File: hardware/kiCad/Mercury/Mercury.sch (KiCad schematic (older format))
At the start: 13 parts

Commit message: VDDA
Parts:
- added C?: 1uF, symbol Device:C_Small
- added C?: 10nF, symbol Device:C_Small
- added L?: 39nH, symbol Device:L_Small
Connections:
- net +3.3VA: now also C?.1, C?.1, L?.2
- net +3V3: now also L?.1
- net GND: now also C?.2, C?.2
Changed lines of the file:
@@
 $EndComp
 Connection ~ 1900 1550
+$Comp
+L Device:L_Small L?
+U 1 1 5FE2984C
+P 5050 1150
+F 0 "L?" V 5250 1200 50  0000 C CNN
+F 1 "39nH" V 5150 1200 50  0000 C CNN
+F 2 "" H 5050 1150 50  0001 C CNN
+F 3 "~" H 5050 1150 50  0001 C CNN
+	1    5050 1150
+	0    -1   -1   0
+$EndComp
+$Comp
+L power:+3.3V #PWR?
+U 1 1 5FE29DC7
+P 4750 1100
+F 0 "#PWR?" H 4750 950 50  0001 C CNN
+F 1 "+3.3V" H 4765 1273 50  0000 C CNN
+F 2 "" H 4750 1100 50  0001 C CNN
+F 3 "" H 4750 1100 50  0001 C CNN
+	1    4750 1100
+	1    0    0    -1
+$EndComp
+Wire Wire Line
+	4750 1100 4750 1150
+Wire Wire Line
+	4750 1150 4950 1150
+$Comp
+L Device:C_Small C?
+U 1 1 5FE2B6A9
+P 5200 1250
+F 0 "C?" H 5150 1450 50  0000 L CNN
+F 1 "1uF" H 5100 1050 50  0000 L CNN
+F 2 "" H 5200 1250 50  0001 C CNN
+F 3 "~" H 5200 1250 50  0001 C CNN
+	1    5200 1250
+	1    0    0    -1
+$EndComp
+$Comp
+L Device:C_Small C?
+U 1 1 5FE2BF87
+P 5450 1250
+F 0 "C?" H 5400 1450 50  0000 L CNN
+F 1 "10nF" H 5350 1050 50  0000 L CNN
+F 2 "" H 5450 1250 50  0001 C CNN
+F 3 "~" H 5450 1250 50  0001 C CNN
+	1    5450 1250
+	1    0    0    -1
+$EndComp
+Wire Wire Line
+	5150 1150 5200 1150
+Wire Wire Line
+	5200 1150 5450 1150
+Connection ~ 5200 1150
+Wire Wire Line
+	5200 1350 5300 1350
+$Comp
+L power:+3.3VA #PWR?
+U 1 1 5FE3082E
+P 5600 1100
+F 0 "#PWR?" H 5600 950 50  0001 C CNN
+F 1 "+3.3VA" H 5615 1273 50  0000 C CNN
+F 2 "" H 5600 1100 50  0001 C CNN
+F 3 "" H 5600 1100 50  0001 C CNN
+	1    5600 1100
+	1    0    0    -1
+$EndComp
+Wire Wire Line
+	5450 1150 5600 1150
+Wire Wire Line
+	5600 1150 5600 1100
+Connection ~ 5450 1150
+$Comp
+L power:GND #PWR?
+U 1 1 5FE32675
+P 5300 1450
+F 0 "#PWR?" H 5300 1200 50  0001 C CNN
+F 1 "GND" H 5305 1277 50  0000 C CNN
+F 2 "" H 5300 1450 50  0001 C CNN
+F 3 "" H 5300 1450 50  0001 C CNN
+	1    5300 1450
+	1    0    0    -1
+$EndComp
+Wire Wire Line
+	5300 1450 5300 1350
+Connection ~ 5300 1350
+Wire Wire Line
+	5300 1350 5450 1350
 $EndSCHEMATC

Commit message: Clock
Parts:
- added C? (x2): 12pF, symbol Device:C_Small
- added R?: 47, symbol Device:R_Small
- added Y?: HSE 16MHz, symbol Device:Crystal_GND24_Small
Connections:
- net GND: now also C?.2, C?.2, Y?.2, Y?.4
- net HSE_OSC_IN: now also C?.1, Y?.1
- net HSE_OSC_OUT: now also R?.2
- new net: C?.1, R?.1, Y?.3
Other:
- moved on the sheet: C?, L?, R?, SW?, U?

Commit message: Added Connectors
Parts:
- added C? (x4): 22uF, symbol Device:C_Small
- added D?: GREEN_LED, symbol Device:LED
- added J?: Battery Input, symbol Connector:Screw_Terminal_01x02
- added J?: SWD, symbol Connector_Generic:Conn_02x05_Odd_Even
- added J? (x2): I2C1, symbol Connector_Generic:Conn_01x04
- added J?: I2C2, symbol Connector_Generic:Conn_01x04
- added J?: USB_C_Receptacle_USB2.0, symbol Connector:USB_C_Receptacle_USB2.0
- added Q?: AO3401A, Package_TO_SOT_SMD:SOT-23, symbol Transistor_FET:AO3401A
- added R?: 1k, symbol Device:R_Small
- added R? (x4): 4k7, symbol Device:R_Small
- added U?: AMS1117-3.3, Package_TO_SOT_SMD:SOT-223-3_TabPin2, symbol Regulator_Linear:AMS1117-3.3
- added U?: AMS1117-5.0, Package_TO_SOT_SMD:SOT-223-3_TabPin2, symbol Regulator_Linear:AMS1117-5.0
- added U?: TUSB320, Package_DFN_QFN:Texas_X2QFN-12_1.6x1.6mm_P0.4mm, symbol Interface_USB:TUSB320
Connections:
- net labels added: +5V, STATUS_LED, V+, Vin
- wire segments 73 -> 127
- no-connect marks 0 -> 2

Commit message: USB CONNECTOR MICROB
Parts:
- removed J?: USB_C_Receptacle_USB2.0, symbol Connector:USB_C_Receptacle_USB2.0
- removed U?: TUSB320, Package_DFN_QFN:Texas_X2QFN-12_1.6x1.6mm_P0.4mm, symbol Interface_USB:TUSB320
- added D?: RED_LED, symbol Device:LED
- added D?: ORANGE_LED, symbol Device:LED
- added J?: USB_B_Micro, symbol Connector:USB_B_Micro
- added R? (x2): 10, symbol Device:R_Small
- added R? (x10): 22, symbol Device:R_Small
- added R? (x2): 1k, symbol Device:R_Small
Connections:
- wire segments 127 -> 139
- no-connect marks 2 -> 6
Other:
- moved on the sheet: D?, J?, R?

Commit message: Peripherals Added
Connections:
- net ALT_INT_2: now reaches U?.45 (PE14)
- net ALT_INT_1: now reaches U?.46 (PE15)
- net FLASH_CS: now reaches U?.51 (PB12)
- net IMU_INT: now reaches U?.91 (PB5)
- no-connect marks 6 -> 5
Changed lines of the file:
@@
 $Descr USLetter 11000 8500
 encoding utf-8
-Sheet 1 1
+Sheet 1 2
 Title "Mercury Avionics Package"
 Date "2020-12-21"
@@
 	0    -1   -1   0
 $EndComp
-NoConn ~ 800  6125
 $Comp
 L Device:LED D?
@@
 	-1   0    0    1
 $EndComp
+$Sheet
+S 6050 4975 1600 800
+U 5FE81F4B
+F0 "peripherals" 50
+F1 "peripherals.sch" 50
+$EndSheet
+Text GLabel 4300 4000 2    50   Input ~ 0
+IMU_INT
+Text GLabel 4300 4700 2    50   Input ~ 0
+FLASH_CS
+Text GLabel 2500 4900 0    50   Input ~ 0
+ALT_INT_2
+Text GLabel 2500 5000 0    50   Input ~ 0
+ALT_INT_1
 $EndSCHEMATC

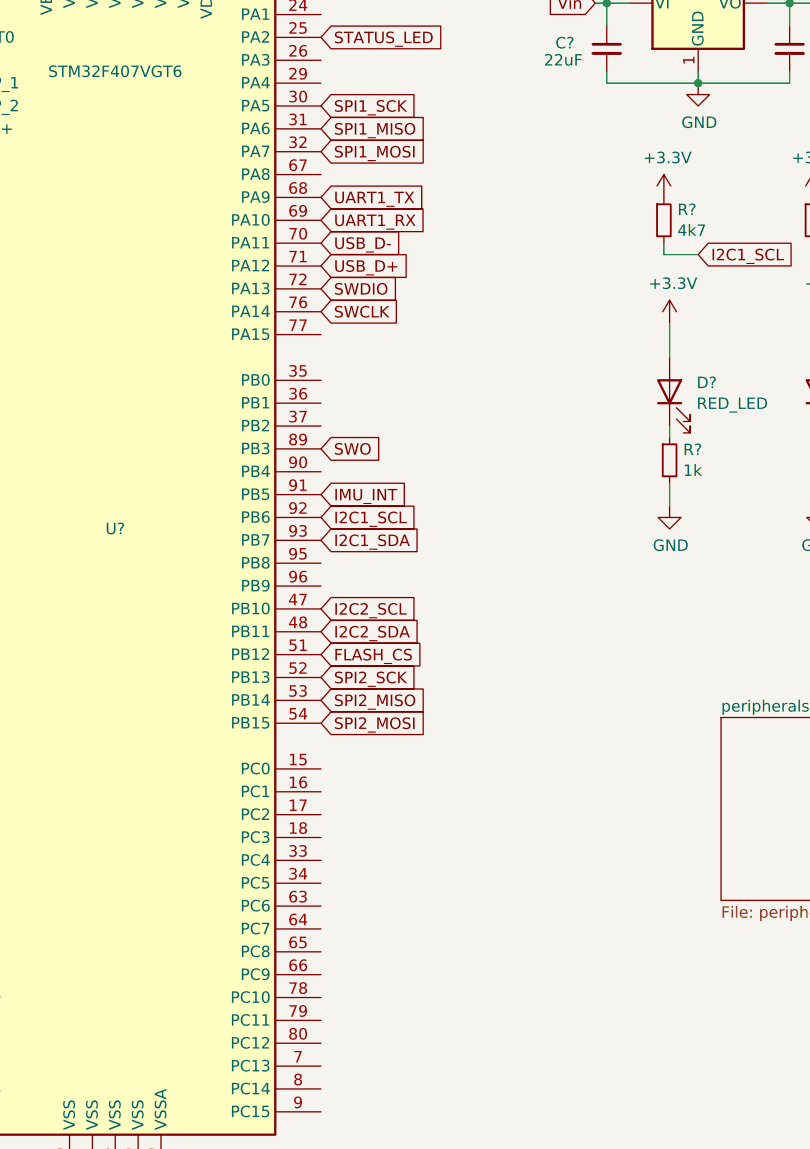
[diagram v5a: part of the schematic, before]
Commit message: GPS MODULE ADDED
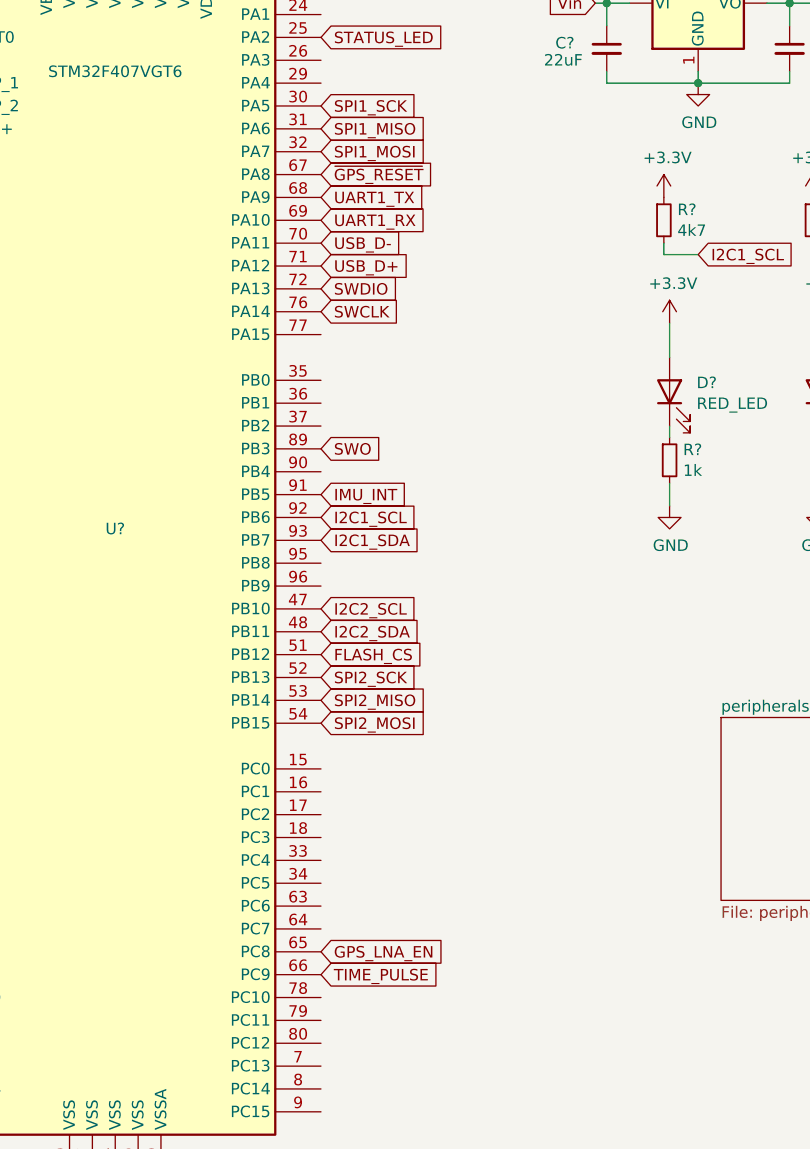
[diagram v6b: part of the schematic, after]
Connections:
- net GPS_LNA_EN: now reaches U?.65 (PC8)
- net TIME_PULSE: now reaches U?.66 (PC9)
- net ~GPS_RESET: now reaches U?.67 (PA8)
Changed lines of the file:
@@
 Text GLabel 2500 5000 0    50   Input ~ 0
 ALT_INT_1
+Text GLabel 4300 2600 2    50   Input ~ 0
+~GPS_RESET
+Text GLabel 4300 6100 2    50   Input ~ 0
+TIME_PULSE
+Text GLabel 4300 6000 2    50   Input ~ 0
+GPS_LNA_EN
 $EndSCHEMATC
